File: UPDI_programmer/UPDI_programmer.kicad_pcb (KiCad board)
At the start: 2 copper layers, 74.3 x 25.4 mm, 30 parts, among them J1 UPDI, J2 ICSP, J3 USB_A, U1 ATmega168P-20AU, U2 FT230XS, Y1 16MHz

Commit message: UPDI PCB RC1
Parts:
- added QR*****: https://tinyurl.com/ghdbks, QR:kicad-simple, B.Cu at (160.0, 61.6)
- added REF**: KiCad-Logo2_5mm_SilkScreen, Symbol:KiCad-Logo2_5mm_SilkScreen, B.Cu at (128.9, 66.0)
- J3: value USB_A -> USB_B; footprint Connector_USB:USB_A_CONNFLY_DS1095-WNR0 -> Connector_USB:USB_B_OST_USB-B1HSxx_Horizontal
- moved JP1 22.9 mm to (150.5, 75.6), turned to 0 degrees
- moved D3 19.7 mm to (107.3, 58.4)
- moved R1 19.7 mm to (113.7, 58.4)
- moved FB1 16.8 mm to (107.3, 77.5), turned to 180 degrees
- moved C9 15.4 mm to (135.3, 58.4)
- moved REF** 14.6 mm to (161.9, 59.7)
- moved C3 11.4 mm to (113.7, 69.8)
- moved R7 11.4 mm to (146.7, 69.8)
- moved J1 9.61 mm to (156.8, 69.8)
- moved C7 7.96 mm to (126.4, 66.0)
- moved C11 7.01 mm to (146.7, 76.8), turned to 270 degrees
- moved U2 6.38 mm to (137.2, 67.3), turned to 90 degrees
- moved J2 4.84 mm to (149.9, 57.1)
- moved U1 4.58 mm to (127.6, 60.3)
- moved Y1 4.49 mm to (136.5, 76.8)
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- renumbered C8 to C1, C4 to C10, C5 to C11, C7 to C2, C6 to C3, C10 to C4, C1 to C5, C9 to C6, C2 to C7, C3 to C8, C11 to C9, R6 to R1, R3 to R2, R2 to R3, R5 to R4, R7 to R5, R4 to R6, R1 to R7, U2 to U1, U1 to U2
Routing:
- net UPDI: track 51.9 -> 14.4 mm, vias 4 -> 0
- net GND: track 58.2 -> 40.1 mm, vias 4 -> 6
- net Net-(J1-Pad1): track 30.3 -> 15.4 mm
- net ~RESET: track 17.4 -> 28.2 mm, vias 0 -> 3
- net Net-(C8-Pad1): track 24.0 -> 17.5 mm
- net USBD+: track 10.1 -> 16.4 mm, vias 0 -> 2
- net Net-(C11-Pad1): track 17.0 -> 11.8 mm
- net MOSI: track 19.3 -> 14.3 mm, vias 1 -> 0
- net MISO: track 19.4 -> 15.0 mm, vias 2 -> 1
- net Net-(C10-Pad2): track 16.5 -> 12.1 mm
- net VCC: track 109.1 -> 113.5 mm
- net Net-(C1-Pad1): track 15.7 -> 19.7 mm
- net ~TXLED: track 10.3 -> 14.3 mm
- net TxD: track 16.2 -> 19.7 mm, vias 0 -> 2
- net Net-(C2-Pad1): track 15.4 -> 18.4 mm
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- added copper zone on B.Cu, net GND
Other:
- board size 74.3 x 25.4 mm -> 67.3 x 25.4 mm
- board text added: "Based on Stefan Wagner’s design https://easyeda.com/wagiminator/y-updi-programmer"
- board text added: "JTAG2UPDI Programmer ver. 1.0 Designed by Dawid Buchwald"
- board text added: "PWR"
- board text added: "RX"
- board text added: "TX"

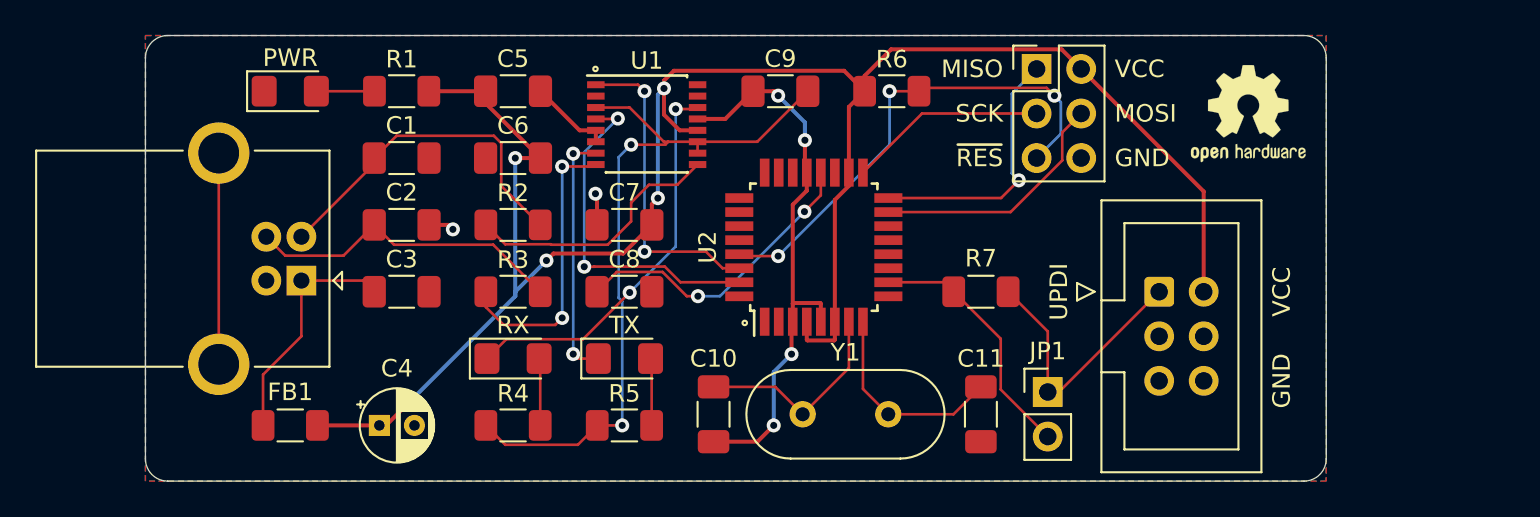
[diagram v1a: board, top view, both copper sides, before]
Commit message: Updated VIA params and changed UPDI resistor
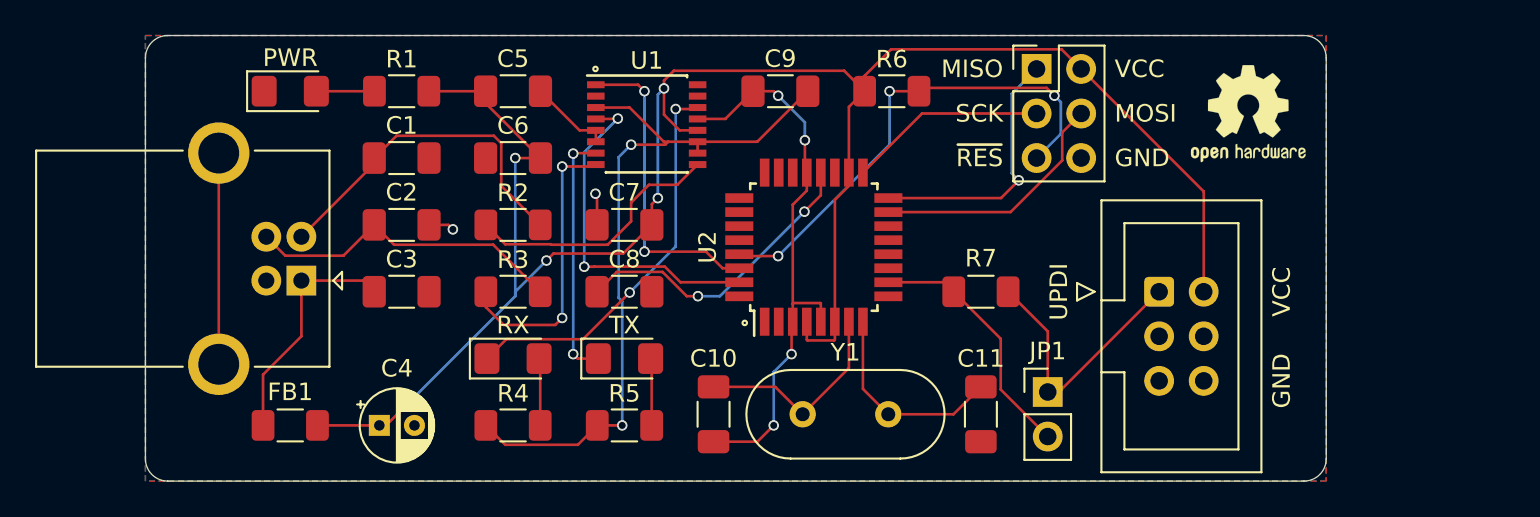
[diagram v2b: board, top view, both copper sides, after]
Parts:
- JP1: value UPDI_R4K7 -> UPDI_R470
- R7: value 4K7 -> 470
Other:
- net class Default: via_dia 0.8 -> 0.6
- net class PWR: via_dia 0.8 -> 0.6
